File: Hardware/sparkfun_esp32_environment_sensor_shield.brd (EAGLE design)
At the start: 58.4 x 50.8 mm, 49 parts, among them J1 WEATHER_METER-WIND, J2 WEATHER_METER-RAIN, U1 BME280, U2 CCS811, U3 APDS-9301, U4 TVS Diode

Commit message: Fix issues from review
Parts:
- added FD3, FD4: FIDUCIAL1X2, SparkFun-Aesthetics:FIDUCIAL-1X2
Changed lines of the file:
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@@
 <grid distance="0.05" unitdist="inch" unit="inch" style="lines" multiple="1" display="yes" altdistance="0.005" altunitdist="inch" altunit="inch"/>
 <layers>
-<layer number="1" name="Top" color="4" fill="1" visible="yes" active="yes"/>
+<layer number="1" name="Top" color="4" fill="1" visible="no" active="yes"/>
 <layer number="2" name="Route2" color="1" fill="3" visible="no" active="yes"/>
 <layer number="15" name="Route15" color="4" fill="6" visible="no" active="yes"/>
@@
 <layer number="19" name="Unrouted" color="6" fill="1" visible="yes" active="yes"/>
 <layer number="20" name="Dimension" color="15" fill="1" visible="yes" active="yes"/>
-<layer number="21" name="tPlace" color="16" fill="1" visible="yes" active="yes"/>
+<layer number="21" name="tPlace" color="16" fill="1" visible="no" active="yes"/>
 <layer number="22" name="bPlace" color="14" fill="1" visible="yes" active="yes"/>
-<layer number="23" name="tOrigins" color="15" fill="1" visible="yes" active="yes"/>
+<layer number="23" name="tOrigins" color="15" fill="1" visible="no" active="yes"/>
 <layer number="24" name="bOrigins" color="15" fill="1" visible="yes" active="yes"/>
 <layer number="25" name="tNames" color="7" fill="1" visible="no" active="yes"/>
@@
 <layer number="43" name="vRestrict" color="2" fill="10" visible="no" active="yes"/>
 <layer number="44" name="Drills" color="7" fill="1" visible="no" active="yes"/>
-<layer number="45" name="Holes" color="7" fill="1" visible="yes" active="yes"/>
+<layer number="45" name="Holes" color="7" fill="1" visible="no" active="yes"/>
 <layer number="46" name="Milling" color="3" fill="1" visible="no" active="yes"/>
 <layer number="47" name="Measures" color="7" fill="1" visible="no" active="yes"/>
 <layer number="48" name="Document" color="7" fill="1" visible="no" active="yes"/>
 <layer number="49" name="Reference" color="7" fill="1" visible="no" active="yes"/>
-<layer number="51" name="tDocu" color="6" fill="1" visible="yes" active="yes"/>
+<layer number="51" name="tDocu" color="6" fill="1" visible="no" active="yes"/>
 <layer number="52" name="bDocu" color="7" fill="1" visible="no" active="yes"/>
 <layer number="3" name="Route3" color="4" fill="3" visible="no" active="no"/>
@@
 <attribute name="PROD_ID" value="IC-13662" x="50.673" y="11.43" size="1.778" layer="27" font="vector" ratio="15" rot="R270" display="off"/>
 </element>
+<element name="FD3" library="SparkFun-Aesthetics" package="FIDUCIAL-1X2" value="FIDUCIAL1X2" x="57.15" y="6.35" rot="MR0"/>
+<element name="FD4" library="SparkFun-Aesthetics" package="FIDUCIAL-1X2" value="FIDUCIAL1X2" x="6.35" y="48.26" rot="MR0"/>
 </elements>
 <signals>

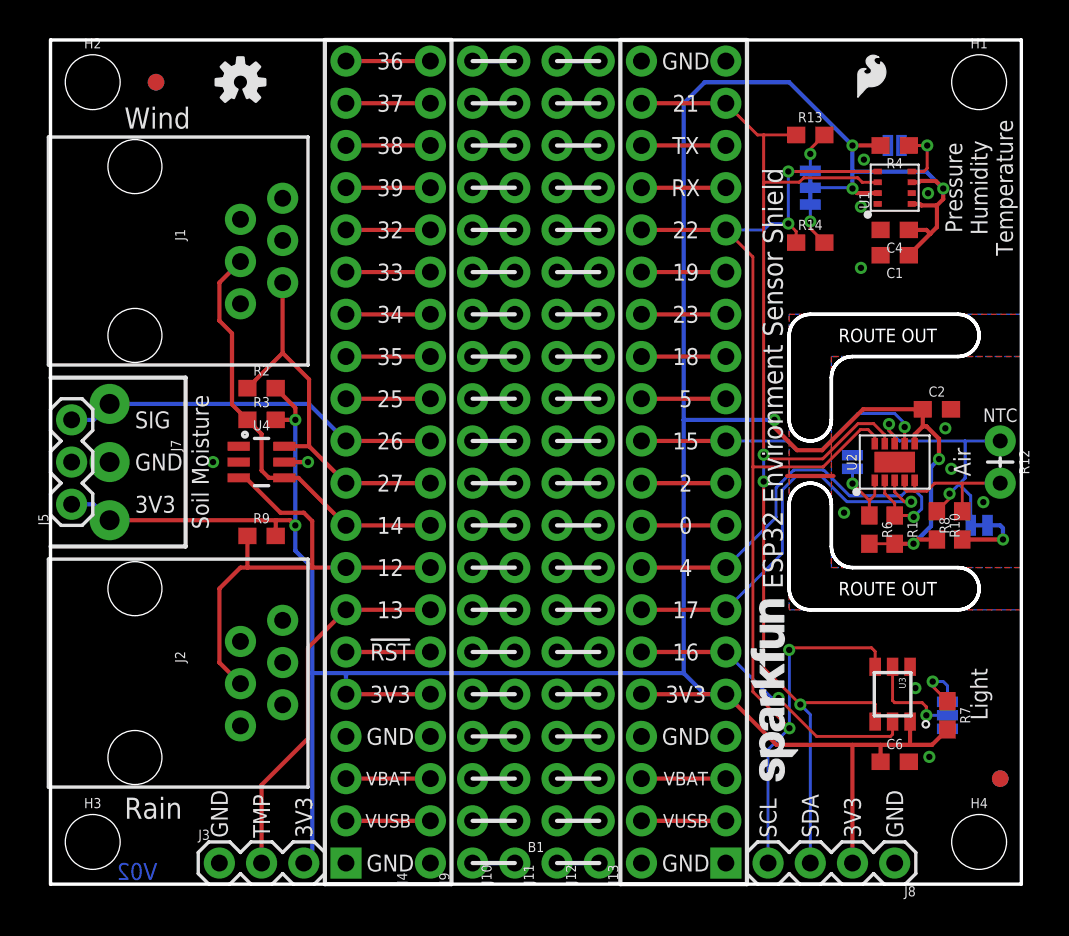
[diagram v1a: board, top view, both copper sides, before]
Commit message: Changes after review of 02  - Change i2c addr info for apds-9301  - Change pin rain sensor is attached to  - Add debounce caps to rain sensor and anemometer  - Fix APDS-9301 footprint
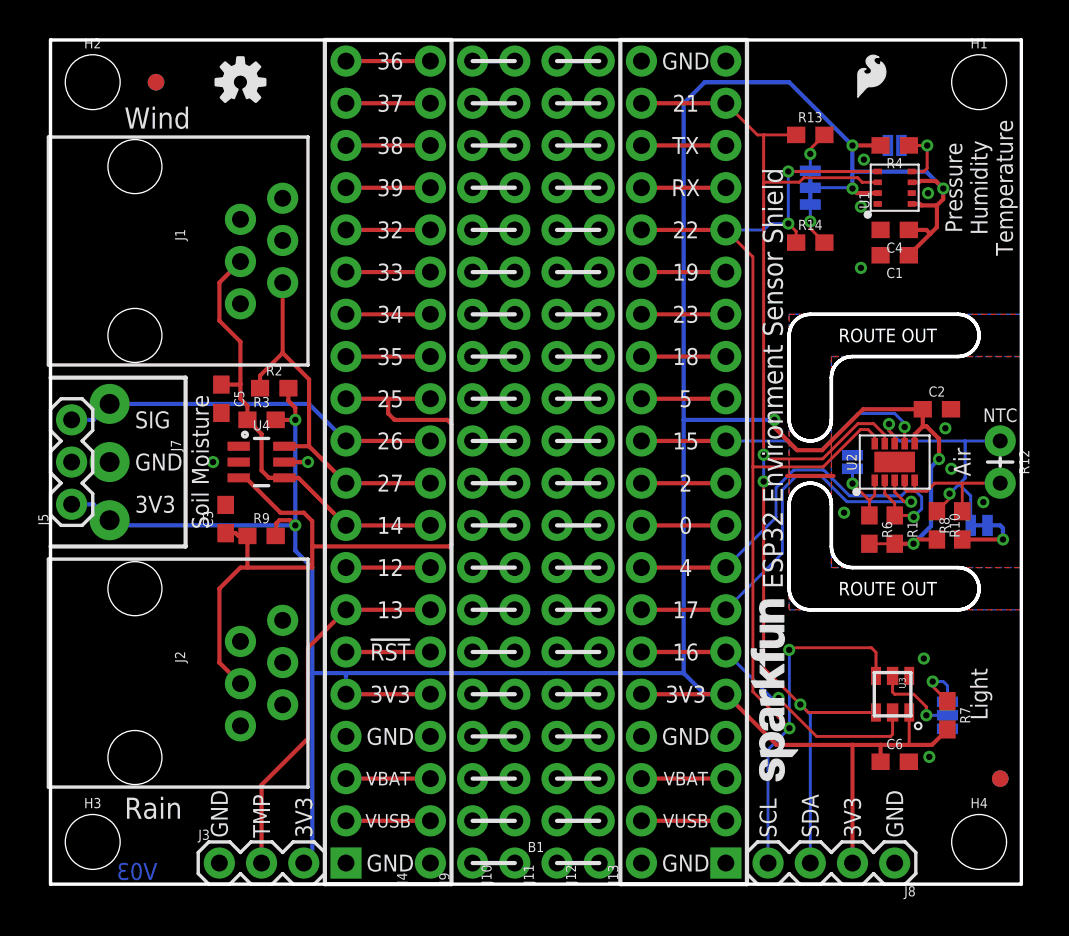
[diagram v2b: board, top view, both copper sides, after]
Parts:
- added C3, C5: 1.0uF, SparkFun-Capacitors:0603
- moved R2 0.76 mm to (13.5, 29.8)
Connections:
- removed net N$9: B1.12, J4.12
- new net N$22: B1.8, J4.8
- net GND: now also C3.2, C5.2
- net RAINFALL: now also B1.12, C3.1, J4.12; no longer B1.8, J4.8
- net WIND_SPEED: now also C5.1
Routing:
- net RAINFALL: track 29.7 -> 49.7 mm
- net N$9: track 5.08 -> 0.00 mm
- net N$22: track 0.00 -> 5.08 mm
- net 3.3V: track 211.3 -> 212.7 mm
- net WIND_SPEED: track 25.7 -> 26.8 mm
- net SDA: track 76.9 -> 76.0 mm
- net ADDR_TSL2561: track 6.00 -> 5.15 mm
- net SCL: track 78.9 -> 79.5 mm
- net LUX_INT: track 18.0 -> 18.6 mm
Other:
- board text added: "V03"
- board text removed: "V02"

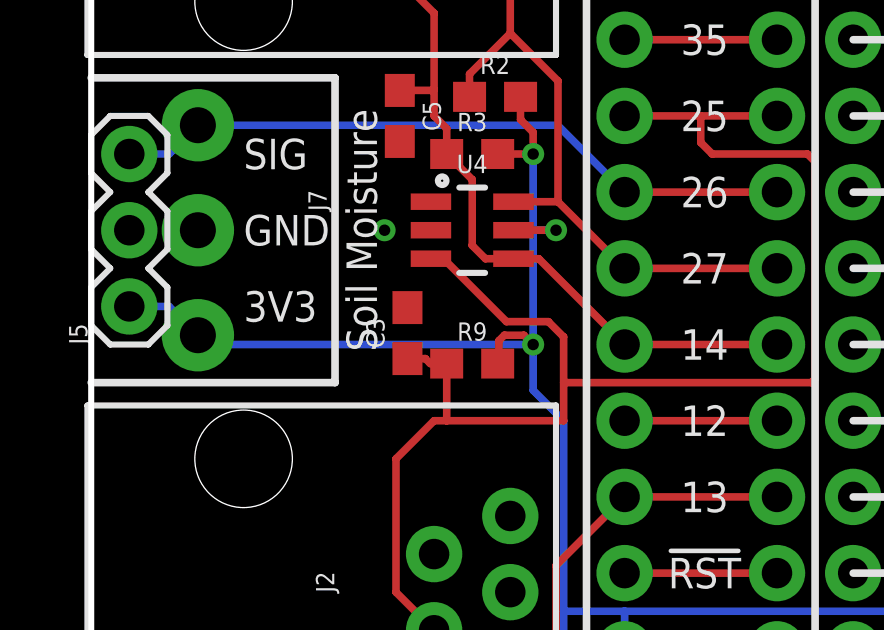
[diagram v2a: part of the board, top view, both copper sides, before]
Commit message: Minor cosmetic changes from review
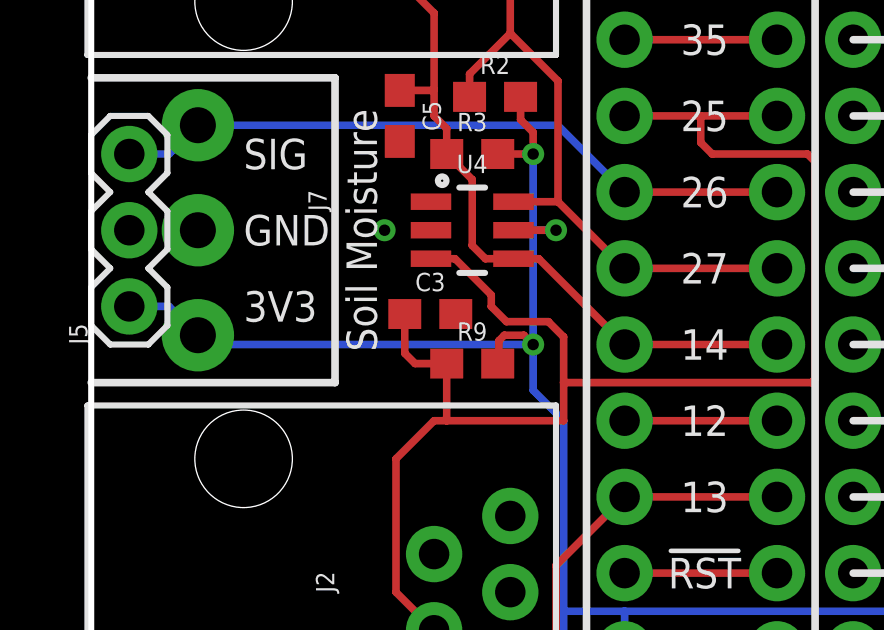
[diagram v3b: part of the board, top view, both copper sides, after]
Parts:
- moved C3 0.99 mm to (11.3, 22.6), turned to 0 degrees
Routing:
- net RAINFALL: track 49.7 -> 51.3 mm
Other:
- board text added: "Jim Lindblom/Mike Hord"
- board text removed: "Jim Lindblom"
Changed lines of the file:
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@@
 <layer number="20" name="Dimension" color="15" fill="1" visible="yes" active="yes"/>
 <layer number="21" name="tPlace" color="16" fill="1" visible="yes" active="yes"/>
-<layer number="22" name="bPlace" color="14" fill="1" visible="yes" active="yes"/>
+<layer number="22" name="bPlace" color="14" fill="1" visible="no" active="yes"/>
 <layer number="23" name="tOrigins" color="15" fill="1" visible="yes" active="yes"/>
-<layer number="24" name="bOrigins" color="15" fill="1" visible="yes" active="yes"/>
-<layer number="25" name="tNames" color="7" fill="1" visible="no" active="yes"/>
+<layer number="24" name="bOrigins" color="15" fill="1" visible="no" active="yes"/>
+<layer number="25" name="tNames" color="7" fill="1" visible="yes" active="yes"/>
 <layer number="26" name="bNames" color="7" fill="1" visible="no" active="yes"/>
 <layer number="27" name="tValues" color="7" fill="1" visible="no" active="yes"/>
@@
 <layer number="43" name="vRestrict" color="2" fill="10" visible="no" active="yes"/>
 <layer number="44" name="Drills" color="7" fill="1" visible="no" active="yes"/>
-<layer number="45" name="Holes" color="7" fill="1" visible="yes" active="yes"/>
+<layer number="45" name="Holes" color="7" fill="1" visible="no" active="yes"/>
 <layer number="46" name="Milling" color="3" fill="1" visible="no" active="yes"/>
 <layer number="47" name="Measures" color="7" fill="1" visible="no" active="yes"/>
 <layer number="48" name="Document" color="7" fill="1" visible="no" active="yes"/>
 <layer number="49" name="Reference" color="7" fill="1" visible="no" active="yes"/>
-<layer number="51" name="tDocu" color="6" fill="1" visible="yes" active="yes"/>
+<layer number="51" name="tDocu" color="6" fill="1" visible="no" active="yes"/>
 <layer number="52" name="bDocu" color="7" fill="1" visible="no" active="yes"/>
 <layer number="3" name="Route3" color="4" fill="3" visible="no" active="no"/>
@@
 <text x="55.88" y="20.32" size="0.889" layer="22" ratio="15" rot="MR180" align="bottom-center">JP4</text>
 <text x="46.863" y="41.91" size="0.889" layer="22" ratio="15" rot="MR90" align="bottom-center">JP5</text>
-<text x="16.51" y="-21.59" size="1.778" layer="51">Jim Lindblom</text>
+<text x="16.51" y="-21.59" size="1.778" layer="51">Jim Lindblom/Mike Hord</text>
 <wire x1="25.4" y1="1.27" x2="27.94" y2="1.27" width="0.254" layer="21"/>
 <wire x1="25.4" y1="3.81" x2="27.94" y2="3.81" width="0.254" layer="21"/>
@@
 <element name="FD3" library="SparkFun-Aesthetics" package="FIDUCIAL-1X2" value="FIDUCIAL1X2" x="57.15" y="6.35" rot="MR0"/>
 <element name="FD4" library="SparkFun-Aesthetics" package="FIDUCIAL-1X2" value="FIDUCIAL1X2" x="6.35" y="48.26" rot="MR0"/>
-<element name="C3" library="SparkFun-Capacitors" package="0603" value="1.0uF" x="10.541" y="21.971" rot="R90">
-<attribute name="PROD_ID" value="CAP-00868" x="10.541" y="21.971" size="1.778" layer="27" font="vector" ratio="15" rot="R90" display="off"/>
+<element name="C3" library="SparkFun-Capacitors" package="0603" value="1.0uF" x="11.303" y="22.606">
+<attribute name="PROD_ID" value="CAP-00868" x="11.303" y="22.606" size="1.778" layer="27" font="vector" ratio="15" display="off"/>
 </element>
 <element name="C5" library="SparkFun-Capacitors" package="0603" value="1.0uF" x="10.287" y="29.21" rot="R270">
@@
 <wire x1="11.85" y1="20.955" x2="11.85" y2="19.05" width="0.254" layer="1"/>
 <wire x1="11.85" y1="19.05" x2="11.43" y2="19.05" width="0.254" layer="1"/>
-<wire x1="11.745" y1="24.45" x2="13.843" y2="22.352" width="0.254" layer="1"/>
 <wire x1="13.843" y1="22.352" x2="15.24" y2="22.352" width="0.254" layer="1"/>
 <wire x1="15.24" y1="22.352" x2="15.748" y2="21.844" width="0.254" layer="1"/>
@@
 <contactref element="U4" pad="3"/>
 <wire x1="15.748" y1="20.32" x2="15.748" y2="19.05" width="0.254" layer="1"/>
-<wire x1="11.745" y1="24.45" x2="11.3249" y2="24.45" width="0.254" layer="1"/>
+<wire x1="12.126" y1="24.45" x2="11.3249" y2="24.45" width="0.254" layer="1"/>
 <contactref element="B1" pad="12"/>
 <contactref element="J4" pad="12"/>
@@
 <contactref element="C3" pad="1"/>
 <wire x1="20.32" y1="29.21" x2="17.78" y2="29.21" width="0.254" layer="1"/>
-<wire x1="11.85" y1="20.955" x2="11.303" y2="20.955" width="0.254" layer="1"/>
-<wire x1="11.303" y1="20.955" x2="11.137" y2="21.121" width="0.254" layer="1"/>
-<wire x1="10.541" y1="21.121" x2="11.137" y2="21.121" width="0.254" layer="1"/>
 <wire x1="20.32" y1="29.21" x2="20.32" y2="28.321" width="0.254" layer="1"/>
 <wire x1="20.32" y1="28.321" x2="20.701" y2="27.94" width="0.254" layer="1"/>
@@
 <wire x1="24.13" y1="20.447" x2="24.003" y2="20.32" width="0.254" layer="1"/>
 <wire x1="24.003" y1="20.32" x2="15.748" y2="20.32" width="0.254" layer="1"/>
+<wire x1="12.126" y1="24.45" x2="13.335" y2="23.241" width="0.254" layer="1"/>
+<wire x1="13.335" y1="23.241" x2="13.335" y2="22.86" width="0.254" layer="1"/>
+<wire x1="13.335" y1="22.86" x2="13.843" y2="22.352" width="0.254" layer="1"/>
+<wire x1="10.453" y1="22.606" x2="10.453" y2="21.297" width="0.254" layer="1"/>
+<wire x1="10.453" y1="21.297" x2="10.795" y2="20.955" width="0.254" layer="1"/>
+<wire x1="10.795" y1="20.955" x2="11.85" y2="20.955" width="0.254" layer="1"/>
 </signal>
 <signal name="EXT_TEMPERATURE">

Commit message: Changes from review
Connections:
- removed net N$10: B1.13, J4.13
- new net N$9: B1.10, J4.10
- net WIND_DIR: now also B1.13, J4.13; no longer B1.10, J4.10
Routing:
- net N$9: track 0.00 -> 5.08 mm
- net N$10: track 5.08 -> 0.00 mm
- net 3.3V: track 212.7 -> 213.9 mm
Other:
- board text added: "v10"
- board text removed: "V03"
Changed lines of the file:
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@@
 <text x="3.048" y="38.608" size="1.016" layer="22" ratio="15" rot="MR270" align="bottom-center">ESP32 Environment
 Sensor Shield</text>
-<text x="5.207" y="0.254" size="1.016" layer="16" ratio="15" rot="MR0" align="bottom-center">V03</text>
+<text x="5.207" y="0.254" size="1.016" layer="16" ratio="15" rot="MR0" align="bottom-center">v10</text>
 <text x="49.53" y="25.4" size="0.889" layer="22" ratio="15" rot="MR90" align="bottom-center">JP2</text>
 <text x="50.8" y="45.593" size="0.889" layer="22" ratio="15" rot="MR0" align="bottom-center">JP1</text>
@@
 <text x="41.783" y="46.99" size="0.889" layer="22" font="vector" ratio="15" rot="MR0" align="center-right">SDA</text>
 <text x="16.891" y="17.272" size="0.889" layer="22" font="vector" ratio="15" rot="MR0" align="center-left">TMP</text>
-<text x="16.51" y="19.05" size="0.889" layer="22" font="vector" ratio="15" rot="MR0" align="center-left">RAIN</text>
+<text x="16.51" y="29.21" size="0.889" layer="22" font="vector" ratio="15" rot="MR0" align="center-left">RAIN</text>
 <text x="16.51" y="21.59" size="0.889" layer="22" font="vector" ratio="15" rot="MR0" align="center-left">WIND
 SPEED</text>
-<text x="16.51" y="24.13" size="0.889" layer="22" font="vector" ratio="15" rot="MR0" align="center-left">WIND
+<text x="16.51" y="31.75" size="0.889" layer="22" font="vector" ratio="15" rot="MR0" align="center-left">WIND
 DIR</text>
 <text x="16.51" y="26.67" size="0.889" layer="22" font="vector" ratio="15" rot="MR0" align="center-left">SOIL</text>
@@
 <via x="53.721" y="41.8592" extent="1-16" drill="0.381"/>
 <wire x1="53.721" y1="41.8592" x2="53.2638" y2="42.3164" width="0.254" layer="1"/>
-<wire x1="51.65" y1="37.846" x2="52.9395" y2="39.1355" width="0.254" layer="1"/>
-<wire x1="52.9395" y1="39.1355" x2="53.34" y2="39.536" width="0.254" layer="1"/>
-<wire x1="53.34" y1="39.536" x2="53.34" y2="40.8432" width="0.254" layer="1"/>
-<wire x1="51.65" y1="39.37" x2="52.705" y2="39.37" width="0.254" layer="1"/>
-<wire x1="52.705" y1="39.37" x2="52.9395" y2="39.1355" width="0.254" layer="1"/>
+<wire x1="51.65" y1="39.37" x2="53.34" y2="39.37" width="0.254" layer="1"/>
 <wire x1="1.27" y1="22.86" x2="2.596" y2="22.86" width="0.254" layer="16"/>
 <wire x1="2.596" y1="22.86" x2="3.556" y2="21.9" width="0.254" layer="16"/>
@@
 <wire x1="51.673" y1="10.33" x2="51.673" y2="8.398" width="0.1778" layer="1"/>
 <wire x1="51.673" y1="8.398" x2="51.689" y2="8.382" width="0.1778" layer="1"/>
+<wire x1="53.34" y1="40.8432" x2="53.34" y2="39.37" width="0.254" layer="1"/>
+<wire x1="53.34" y1="39.37" x2="53.34" y2="37.973" width="0.254" layer="1"/>
+<wire x1="53.34" y1="37.973" x2="53.213" y2="37.846" width="0.254" layer="1"/>
+<wire x1="53.213" y1="37.846" x2="51.65" y2="37.846" width="0.254" layer="1"/>
 </signal>
 <signal name="ADDR_TSL2561">
@@
 <contactref element="R2" pad="1"/>
 <contactref element="J1" pad="5"/>
-<contactref element="B1" pad="10"/>
-<contactref element="J4" pad="10"/>
-<wire x1="22.86" y1="24.13" x2="17.78" y2="24.13" width="0.254" layer="1"/>
 <wire x1="13.97" y1="31.965" x2="13.97" y2="36.195" width="0.254" layer="1"/>
-<wire x1="13.97" y1="31.965" x2="15.56" y2="30.375" width="0.254" layer="1"/>
-<wire x1="17.78" y1="24.13" x2="15.56" y2="26.35" width="0.254" layer="1"/>
+<wire x1="13.97" y1="31.965" x2="14.649" y2="31.286" width="0.254" layer="1"/>
 <contactref element="U4" pad="6"/>
+<wire x1="14.649" y1="31.286" x2="15.56" y2="30.375" width="0.254" layer="1"/>
 <wire x1="15.56" y1="26.35" x2="15.56" y2="30.375" width="0.254" layer="1"/>
 <wire x1="14.0751" y1="26.35" x2="15.56" y2="26.35" width="0.254" layer="1"/>
 <wire x1="12.612" y1="29.845" x2="12.612" y2="30.607" width="0.254" layer="1"/>
 <wire x1="12.612" y1="30.607" x2="13.97" y2="31.965" width="0.254" layer="1"/>
+<contactref element="B1" pad="13"/>
+<contactref element="J4" pad="13"/>
+<wire x1="22.86" y1="31.75" x2="17.78" y2="31.75" width="0.254" layer="1"/>
+<wire x1="17.78" y1="31.75" x2="15.113" y2="31.75" width="0.254" layer="1"/>
+<wire x1="15.113" y1="31.75" x2="14.649" y2="31.286" width="0.254" layer="1"/>
 </signal>
 <signal name="WIND_SPEED">
@@
 <contactref element="R13" pad="2"/>
 <contactref element="JP5" pad="3"/>
-<wire x1="46.57" y1="45.085" x2="45.72" y2="44.235" width="0.1778" layer="1"/>
-<wire x1="45.72" y1="44.235" x2="45.72" y2="43.942" width="0.1778" layer="1"/>
 <via x="45.72" y="43.942" extent="1-16" drill="0.381"/>
 <wire x1="45.72" y1="43.942" x2="45.72" y2="42.926" width="0.1778" layer="16"/>
+<wire x1="45.72" y1="43.942" x2="46.355" y2="43.942" width="0.1778" layer="1"/>
+<wire x1="46.355" y1="43.942" x2="46.57" y2="44.157" width="0.1778" layer="1"/>
+<wire x1="46.57" y1="45.085" x2="46.57" y2="44.157" width="0.1778" layer="1"/>
 </signal>
 <signal name="N$5">
 <contactref element="R14" pad="2"/>
 <contactref element="JP5" pad="1"/>
-<wire x1="46.57" y1="38.608" x2="45.72" y2="39.458" width="0.1778" layer="1"/>
-<wire x1="45.72" y1="39.458" x2="45.72" y2="39.878" width="0.1778" layer="1"/>
 <via x="45.72" y="39.878" extent="1-16" drill="0.381"/>
 <wire x1="45.72" y1="39.878" x2="45.72" y2="40.894" width="0.1778" layer="16"/>
+<wire x1="45.72" y1="39.878" x2="46.355" y2="39.878" width="0.1778" layer="1"/>
+<wire x1="46.355" y1="39.878" x2="46.57" y2="39.663" width="0.1778" layer="1"/>
+<wire x1="46.57" y1="38.608" x2="46.57" y2="39.663" width="0.1778" layer="1"/>
 </signal>
 <signal name="N$6">
@@
 <wire x1="22.86" y1="13.97" x2="17.78" y2="13.97" width="0.254" layer="1"/>
 </signal>
-<signal name="N$10">
-<contactref element="B1" pad="13"/>
-<contactref element="J4" pad="13"/>
-<wire x1="22.86" y1="31.75" x2="17.78" y2="31.75" width="0.254" layer="1"/>
-</signal>
 <signal name="N$11">
 <contactref element="B1" pad="14"/>
@@
 <wire x1="17.78" y1="19.05" x2="22.86" y2="19.05" width="0.254" layer="1"/>
 </signal>
+<signal name="N$9">
+<contactref element="J4" pad="10"/>
+<contactref element="B1" pad="10"/>
+<wire x1="22.86" y1="24.13" x2="17.78" y2="24.13" width="0.254" layer="1"/>
+</signal>
 </signals>
